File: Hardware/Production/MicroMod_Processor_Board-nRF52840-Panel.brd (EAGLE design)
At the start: 199.6 x 83.1 mm, 454 parts, among them J1 MICROMOD-2222, J10 MICROMOD-2222, J11 MICROMOD-2222, J12 MICROMOD-2222, J13 MICROMOD-2222, J14 MICROMOD-2222, J15 MICROMOD-2222, J16 MICROMOD-2222, J2 MICROMOD-2222, J3 MICROMOD-2222, J4 MICROMOD-2222, J5 MICROMOD-2222, J6 MICROMOD-2222, J7 MICROMOD-2222, J8 MICROMOD-2222, J9 MICROMOD-2222, U1 W25QXX128MBIT-6X5, U10 MDBT50Q, U11 W25QXX128MBIT-6X5, U12 MDBT50Q, U13 W25QXX128MBIT-6X5, U14 MDBT50Q, U15 W25QXX128MBIT-6X5, U16 MDBT50Q, U17 W25QXX128MBIT-6X5, U18 MDBT50Q, U19 W25QXX128MBIT-6X5, U2 MDBT50Q, U20 MDBT50Q, U21 W25QXX128MBIT-6X5, U22 MDBT50Q, U23 W25QXX128MBIT-6X5, U24 MDBT50Q, U25 W25QXX128MBIT-6X5, U26 MDBT50Q, U27 W25QXX128MBIT-6X5, U28 MDBT50Q, U29 W25QXX128MBIT-6X5, U3 W25QXX128MBIT-6X5, U30 MDBT50Q, U31 W25QXX128MBIT-6X5, U32 MDBT50Q, U4 MDBT50Q, U5 W25QXX128MBIT-6X5, U6 MDBT50Q, U7 W25QXX128MBIT-6X5, U8 MDBT50Q, U9 W25QXX128MBIT-6X5, Y1 32.768kHz, Y10 32.768kHz, Y11 32.768kHz, Y12 32.768kHz, Y13 32.768kHz, Y14 32.768kHz, Y15 32.768kHz, Y16 32.768kHz, Y2 32.768kHz, Y3 32.768kHz, Y4 32.768kHz, Y5 32.768kHz, Y6 32.768kHz, Y7 32.768kHz, Y8 32.768kHz, Y9 32.768kHz

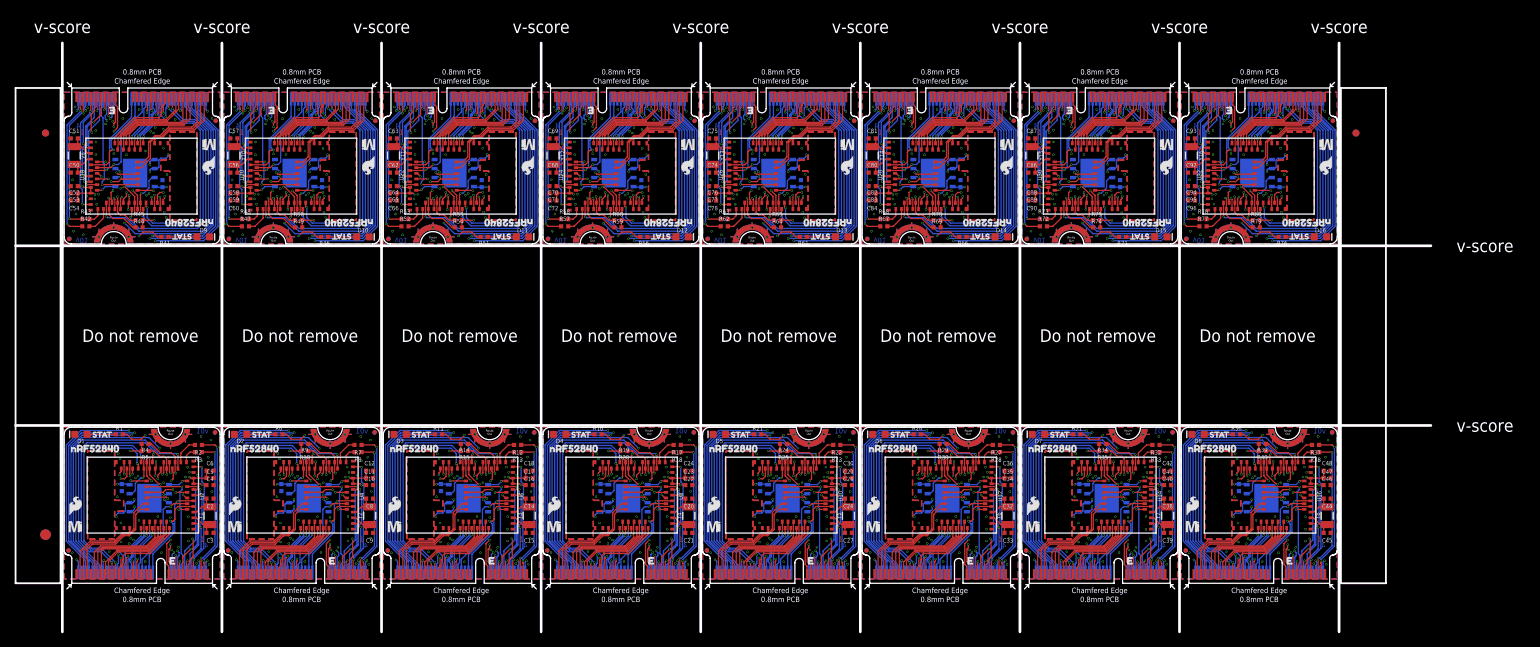
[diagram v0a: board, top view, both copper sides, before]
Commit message: Re-panelized for v10
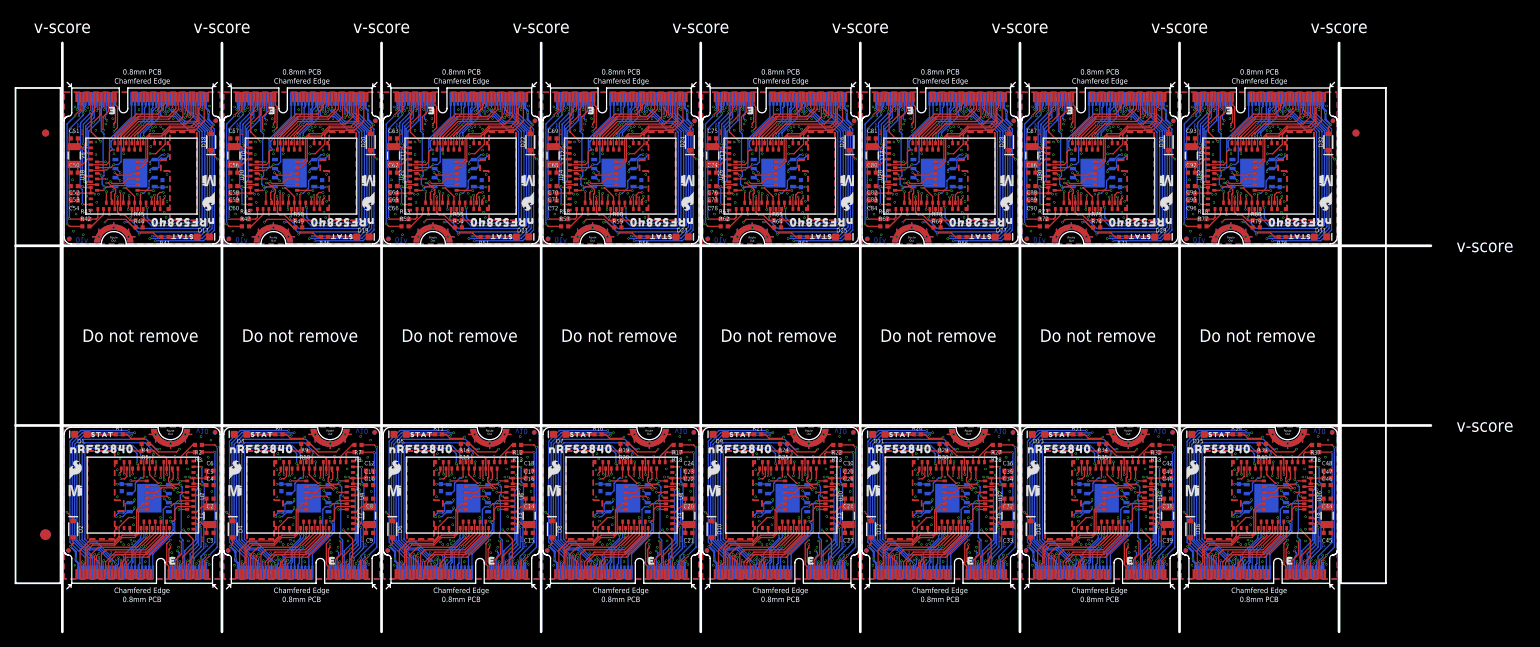
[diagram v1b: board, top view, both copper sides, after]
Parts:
- added D17, D19, D21, D23, D25, D27, D29, D31: BLUE, SparkFun-LED:LED-0603
- added D18, D20, D22, D24, D26, D28, D30, D32: 1A/23V/620mV, SparkFun-DiscreteSemi:SOD-323
- D10, D12, D14, D16, D2, D4, D6, D8: value BLUE -> 1A/23V/620mV; device SparkFun-LED:LED-0603 -> SparkFun-DiscreteSemi:SOD-323
- U$10, U$15, U$20, U$25, U$30, U$35, U$40, U$45, U$50, U$55, U$60, U$65, U$70, U$75, U$80: device buzzard_labels (80):NRF528400 -> output:STAT0
- U$11, U$16, U$21, U$26, U$31, U$36, U$4, U$41, U$46, U$51, U$56, U$61, U$66, U$71, U$76: device SparkFun-Buzzard:STAT_TO_32 -> SparkFun-MicroMod:MICROMOD_MI_LOGO_.35
- U$12, U$17, U$22, U$27, U$32, U$37, U$42, U$47, U$52, U$57, U$62, U$67, U$7, U$72, U$77: device SparkFun-MicroMod:MICROMOD_MI_LOGO_.35 -> SparkFun-MicroMod:MICROMOD_LOGO_.35
- U$13, U$18, U$23, U$28, U$33, U$38, U$43, U$48, U$53, U$58, U$63, U$68, U$73, U$78, U$8: device SparkFun-MicroMod:MICROMOD_LOGO_.35 -> output:NRF528400
- U$14, U$19, U$24, U$29, U$34, U$39, U$44, U$49, U$54, U$59, U$64, U$69, U$74, U$79, U$9: device buzzard_labels (79):NRF528400 -> output:NRF528400
- U$2: device buzzard_labels (79):NRF528400 -> output:STAT0
- U$3: device buzzard_labels (80):NRF528400 -> output:NRF528400
- U$6: device SparkFun-Buzzard:STAT_TO_32 -> output:NRF528400
- moved D8 92.1 mm to (68.8, 7.62), turned to 270 degrees
- moved D9 77.9 mm to (92.4, 21.0), turned to 180 degrees
- moved D6 69.9 mm to (46.3, 7.62), turned to 270 degrees
- moved D7 67.5 mm to (69.9, 21.0)
- moved D10 64.2 mm to (91.3, 7.62), turned to 270 degrees
- moved D11 57.5 mm to (114.9, 21.0), turned to 180 degrees
- moved D12 49.1 mm to (113.8, 7.62), turned to 270 degrees
- moved D4 48.0 mm to (23.8, 7.62), turned to 270 degrees
- moved D16 45.1 mm to (158.8, 7.62), turned to 270 degrees
- moved D5 45.0 mm to (47.4, 21.0)
- moved D14 41.4 mm to (136.3, 7.62), turned to 270 degrees
- moved D13 39.3 mm to (137.4, 21.0), turned to 180 degrees
- moved D15 28.3 mm to (159.9, 21.0), turned to 180 degrees
- moved D2 27.1 mm to (1.27, 7.62), turned to 270 degrees
- moved D3 22.5 mm to (24.9, 21.0)
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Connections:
- net SPI_!CS!16 renamed SPI_!CS1!/SDIO_DATA9
- net SPI_!CS!18 renamed SPI_!CS1!/SDIO_DATA10
- net SPI_!CS!20 renamed SPI_!CS1!/SDIO_DATA11
- net SPI_!CS!22 renamed SPI_!CS1!/SDIO_DATA12
- net SPI_!CS!24 renamed SPI_!CS1!/SDIO_DATA13
- net SPI_!CS!26 renamed SPI_!CS1!/SDIO_DATA14
- net SPI_!CS!28 renamed SPI_!CS1!/SDIO_DATA15
- net SPI_!CS!30 renamed SPI_!CS1!/SDIO_DATA16
- net SPI_MISO1 renamed SPI_CIPO
- net SPI_MISO11 renamed SPI_CIPO5
- net SPI_MISO13 renamed SPI_CIPO6
- net SPI_MISO15 renamed SPI_CIPO7
- net SPI_MISO17 renamed SPI_CIPO8
- net SPI_MISO19 renamed SPI_CIPO9
- net SPI_MISO21 renamed SPI_CIPO10
- net SPI_MISO23 renamed SPI_CIPO11
- net SPI_MISO25 renamed SPI_CIPO12
- net SPI_MISO27 renamed SPI_CIPO13
- net SPI_MISO29 renamed SPI_CIPO14
- net SPI_MISO3 renamed SPI_CIPO1
- net SPI_MISO31 renamed SPI_CIPO15
- net SPI_MISO5 renamed SPI_CIPO2
- net SPI_MISO7 renamed SPI_CIPO3
- net SPI_MISO9 renamed SPI_CIPO4
- net SPI_MOSI1 renamed SPI_COPI
- net SPI_MOSI10 renamed SPI_COPI5
- net SPI_MOSI12 renamed SPI_COPI6
- net SPI_MOSI14 renamed SPI_COPI7
- net SPI_MOSI16 renamed SPI_COPI8
- net SPI_MOSI18 renamed SPI_COPI9
- net SPI_MOSI2 renamed SPI_COPI1
- net SPI_MOSI20 renamed SPI_COPI10
- net SPI_MOSI22 renamed SPI_COPI11
- net SPI_MOSI24 renamed SPI_COPI12
- net SPI_MOSI26 renamed SPI_COPI13
- net SPI_MOSI28 renamed SPI_COPI14
- net SPI_MOSI30 renamed SPI_COPI15
- net SPI_MOSI4 renamed SPI_COPI2
- net SPI_MOSI6 renamed SPI_COPI3
- net SPI_MOSI8 renamed SPI_COPI4
- net SPI_SCK17 renamed SPI_SCK1/SDIO_CLK8
- net SPI_SCK19 renamed SPI_SCK1/SDIO_CLK9
- net SPI_SCK21 renamed SPI_SCK1/SDIO_CLK10
- net SPI_SCK23 renamed SPI_SCK1/SDIO_CLK11
- net SPI_SCK25 renamed SPI_SCK1/SDIO_CLK12
- net SPI_SCK27 renamed SPI_SCK1/SDIO_CLK13
- net SPI_SCK29 renamed SPI_SCK1/SDIO_CLK14
- net SPI_SCK31 renamed SPI_SCK1/SDIO_CLK15
- removed net ADC_D+: J1.63, U2.10
- removed net ADC_D+1: J2.63, U4.10
- removed net ADC_D+10: J11.63, U22.10
- removed net ADC_D+11: J12.63, U24.10
- removed net ADC_D+12: J13.63, U26.10
- removed net ADC_D+13: J14.63, U28.10
- removed net ADC_D+14: J15.63, U30.10
- removed net ADC_D+15: J16.63, U32.10
- removed net ADC_D+2: J3.63, U6.10
- removed net ADC_D+3: J4.63, U8.10
- removed net ADC_D+4: J5.63, U10.10
- removed net ADC_D+5: J6.63, U12.10
- removed net ADC_D+6: J7.63, U14.10
- removed net ADC_D+7: J8.63, U16.10
- removed net ADC_D+8: J9.63, U18.10
- removed net ADC_D+9: J10.63, U20.10
- removed net ADC_D-: J1.65, U2.9
- removed net ADC_D-1: J2.65, U4.9
- removed net ADC_D-10: J11.65, U22.9
- removed net ADC_D-11: J12.65, U24.9
- removed net ADC_D-12: J13.65, U26.9
- removed net ADC_D-13: J14.65, U28.9
- removed net ADC_D-14: J15.65, U30.9
- removed net ADC_D-15: J16.65, U32.9
- removed net ADC_D-2: J3.65, U6.9
- removed net ADC_D-3: J4.65, U8.9
- removed net ADC_D-4: J5.65, U10.9
- removed net ADC_D-5: J6.65, U12.9
- removed net ADC_D-6: J7.65, U14.9
- removed net ADC_D-7: J8.65, U16.9
- removed net ADC_D-8: J9.65, U18.9
- removed net ADC_D-9: J10.65, U20.9
- removed net GPIO0: J1.40, U2.8
- removed net GPIO113: J15.69, U30.56
- removed net GPIO114: J15.71, U30.57
- removed net GPIO115: J15.42, U30.7
- removed net GPIO116: J15.46, U30.5
- removed net GPIO117: J15.44, U30.6
- removed net GPIO118: J15.48, U30.4
- removed net GPIO119: J15.40, U30.8
- removed net GPIO120: J16.73, U32.3
- removed net GPIO121: J16.69, U32.56
- removed net GPIO122: J16.71, U32.57
- removed net GPIO123: J16.42, U32.7
- removed net GPIO124: J16.46, U32.5
- removed net GPIO125: J16.44, U32.6
- removed net GPIO126: J16.48, U32.4
- removed net GPIO127: J16.40, U32.8
- removed net N$11 (its old number): D3.A, R11.1
- removed net N$16 (its old number): D4.A, R16.1
- removed net N$21 (its old number): D5.A, R21.1
- removed net N$26 (its old number): D6.A, R26.1
- removed net N$41 (its old number): D9.A, R41.1
- removed net N$46 (its old number): D10.A, R46.1
- removed net N$51 (its old number): D11.A, R51.1
- removed net N$56 (its old number): D12.A, R56.1
- removed net N$71 (its old number): D15.A, R71.1
- removed net N$76 (its old number): D16.A, R76.1
- removed net NFC1: J1.43, U2.52
- removed net NFC10: J5.41, U10.54
- removed net NFC11: J6.43, U12.52
- removed net NFC12: J6.41, U12.54
- removed net NFC13: J7.43, U14.52
- removed net NFC14: J7.41, U14.54
- removed net NFC15: J8.43, U16.52
- removed net NFC16: J8.41, U16.54
- removed net NFC17: J9.43, U18.52
- removed net NFC18: J9.41, U18.54
- removed net NFC19: J10.43, U20.52
- removed net NFC2: J1.41, U2.54
- removed net NFC20: J10.41, U20.54
- removed net NFC21: J11.43, U22.52
- removed net NFC22: J11.41, U22.54
- removed net NFC23: J12.43, U24.52
- removed net NFC24: J12.41, U24.54
- removed net NFC25: J13.43, U26.52
- removed net NFC26: J13.41, U26.54
- removed net NFC27: J14.43, U28.52
- removed net NFC28: J14.41, U28.54
- removed net NFC29: J15.43, U30.52
- removed net NFC3: J2.43, U4.52
- removed net NFC30: J15.41, U30.54
- removed net NFC31: J16.43, U32.52
- removed net NFC32: J16.41, U32.54
- removed net NFC4: J2.41, U4.54
- removed net NFC5: J3.43, U6.52
- removed net NFC6: J3.41, U6.54
- removed net NFC7: J4.43, U8.52
- removed net NFC8: J4.41, U8.54
- removed net NFC9: J5.43, U10.52
- removed net SPI_!CS!17: J9.55, U18.44
- removed net SPI_!CS!19: J10.55, U20.44
- removed net SPI_!CS!21: J11.55, U22.44
- removed net SPI_!CS!23: J12.55, U24.44
- removed net SPI_!CS!25: J13.55, U26.44
- removed net SPI_!CS!27: J14.55, U28.44
- removed net SPI_!CS!29: J15.55, U30.44
- removed net SPI_!CS!31: J16.55, U32.44
- removed net SPI_MISO: J1.64, U1.5, U2.43
- removed net SPI_MISO10: J6.64, U11.5, U12.43
- removed net SPI_MISO12: J7.64, U13.5, U14.43
- removed net SPI_MISO14: J8.64, U15.5, U16.43
- removed net SPI_MISO16: J9.64, U17.5, U18.43
- removed net SPI_MISO18: J10.64, U19.5, U20.43
- removed net SPI_MISO2: J2.64, U3.5, U4.43
- removed net SPI_MISO20: J11.64, U21.5, U22.43
- removed net SPI_MISO22: J12.64, U23.5, U24.43
- removed net SPI_MISO24: J13.64, U25.5, U26.43
- removed net SPI_MISO26: J14.64, U27.5, U28.43
- removed net SPI_MISO28: J15.64, U29.5, U30.43
- removed net SPI_MISO30: J16.64, U31.5, U32.43
- removed net SPI_MISO4: J3.64, U5.5, U6.43
- removed net SPI_MISO6: J4.64, U7.5, U8.43
- removed net SPI_MISO8: J5.64, U10.43, U9.5
- removed net SPI_MOSI: J1.62, U2.36
- removed net SPI_MOSI11: J6.62, U12.36
- removed net SPI_MOSI13: J7.62, U14.36
- removed net SPI_MOSI15: J8.62, U16.36
- removed net SPI_MOSI17: J9.62, U18.36
- removed net SPI_MOSI19: J10.62, U20.36
- removed net SPI_MOSI21: J11.62, U22.36
- removed net SPI_MOSI23: J12.62, U24.36
- removed net SPI_MOSI25: J13.62, U26.36
- removed net SPI_MOSI27: J14.62, U28.36
- removed net SPI_MOSI29: J15.62, U30.36
- removed net SPI_MOSI3: J2.62, U4.36
- removed net SPI_MOSI31: J16.62, U32.36
- removed net SPI_MOSI5: J3.62, U6.36
- removed net SPI_MOSI7: J4.62, U8.36
- removed net SPI_MOSI9: J5.62, U10.36
- removed net SPI_SCK16: J9.57, U18.13
- removed net SPI_SCK18: J10.57, U20.13
- removed net SPI_SCK20: J11.57, U22.13
- removed net SPI_SCK22: J12.57, U24.13
- removed net SPI_SCK24: J13.57, U26.13
- removed net SPI_SCK26: J14.57, U28.13
- removed net SPI_SCK28: J15.57, U30.13
- removed net SPI_SCK30: J16.57, U32.13
- new net 3.3V_EN: J1.4, U2.8
- new net 3.3V_EN1: J2.4, U4.8
- new net 3.3V_EN10: J11.4, U22.8
- new net 3.3V_EN11: J12.4, U24.8
- new net 3.3V_EN12: J13.4, U26.8
- new net 3.3V_EN13: J14.4, U28.8
- new net 3.3V_EN14: J15.4, U30.8
- new net 3.3V_EN15: J16.4, U32.8
- new net 3.3V_EN2: J3.4, U6.8
- new net 3.3V_EN3: J4.4, U8.8
- new net 3.3V_EN4: J5.4, U10.8
- new net 3.3V_EN5: J6.4, U12.8
- new net 3.3V_EN6: J7.4, U14.8
- new net 3.3V_EN7: J8.4, U16.8
- new net 3.3V_EN8: J9.4, U18.8
- new net 3.3V_EN9: J10.4, U20.8
- new net GPIO0/ADC1: J2.40, U4.10
- new net GPIO0/ADC10: J10.40, U20.10
- new net GPIO0/ADC11: J11.40, U22.10
- new net GPIO0/ADC12: J12.40, U24.10
- new net GPIO0/ADC13: J13.40, U26.10
- new net GPIO0/ADC14: J14.40, U28.10
- new net GPIO0/ADC15: J15.40, U30.10
- new net GPIO0/ADC16: J16.40, U32.10
- new net GPIO0/ADC2: J1.40, U2.10
- new net GPIO0/ADC3: J3.40, U6.10
- new net GPIO0/ADC4: J4.40, U8.10
- new net GPIO0/ADC5: J5.40, U10.10
- new net GPIO0/ADC6: J6.40, U12.10
- new net GPIO0/ADC7: J7.40, U14.10
- new net GPIO0/ADC8: J8.40, U16.10
- new net GPIO0/ADC9: J9.40, U18.10
- new net GPIO1/ADC1: J2.42, U4.9
- new net GPIO1/ADC10: J10.42, U20.9
- new net GPIO1/ADC11: J11.42, U22.9
- new net GPIO1/ADC12: J12.42, U24.9
- new net GPIO1/ADC13: J13.42, U26.9
- new net GPIO1/ADC14: J14.42, U28.9
- new net GPIO1/ADC15: J15.42, U30.9
- new net GPIO1/ADC16: J16.42, U32.9
- new net GPIO1/ADC2: J3.42, U6.9
- new net GPIO1/ADC3: J1.42, U2.9
- new net GPIO1/ADC4: J4.42, U8.9
- new net GPIO1/ADC5: J5.42, U10.9
- new net GPIO1/ADC6: J6.42, U12.9
- new net GPIO1/ADC7: J7.42, U14.9
- new net GPIO1/ADC8: J8.42, U16.9
- new net GPIO1/ADC9: J9.42, U18.9
- new net GPIO10/NFC1: J2.63, U4.54
- new net GPIO10/NFC10: J10.63, U20.54
- new net GPIO10/NFC11: J11.63, U22.54
- new net GPIO10/NFC12: J12.63, U24.54
- new net GPIO10/NFC13: J13.63, U26.54
- new net GPIO10/NFC14: J14.63, U28.54
- new net GPIO10/NFC15: J15.63, U30.54
- new net GPIO10/NFC16: J16.63, U32.54
- new net GPIO10/NFC2: J1.63, U2.54
- new net GPIO10/NFC3: J3.63, U6.54
- new net GPIO10/NFC4: J4.63, U8.54
- new net GPIO10/NFC5: J5.63, U10.54
- new net GPIO10/NFC6: J6.63, U12.54
- new net GPIO10/NFC7: J7.63, U14.54
- new net GPIO10/NFC8: J8.63, U16.54
- new net GPIO10/NFC9: J9.63, U18.54
- new net GPIO9/NFC1: J1.65, U2.52
- new net GPIO9/NFC10: J10.65, U20.52
- new net GPIO9/NFC11: J11.65, U22.52
- new net GPIO9/NFC12: J12.65, U24.52
- new net GPIO9/NFC13: J13.65, U26.52
- new net GPIO9/NFC14: J14.65, U28.52
- new net GPIO9/NFC15: J15.65, U30.52
- new net GPIO9/NFC16: J16.65, U32.52
- new net GPIO9/NFC2: J2.65, U4.52
- new net GPIO9/NFC3: J3.65, U6.52
- new net GPIO9/NFC4: J4.65, U8.52
- new net GPIO9/NFC5: J5.65, U10.52
- new net GPIO9/NFC6: J6.65, U12.52
- new net GPIO9/NFC7: J7.65, U14.52
- new net GPIO9/NFC8: J8.65, U16.52
- new net GPIO9/NFC9: J9.65, U18.52
- new net N$12: D4.A, J2.2, J2.74
- new net N$13: D5.A, R11.1
- new net N$18: D6.A, J3.2, J3.74
- new net N$19: D7.A, R16.1
- new net N$24: D8.A, J4.2, J4.74
- new net N$25: D9.A, R21.1
- new net N$30: D10.A, J5.2, J5.74
- new net N$37: D13.A, R31.1
- new net N$42: D14.A, J7.2, J7.74
- new net N$43: D15.A, R36.1
- new net N$48: D16.A, J8.2, J8.74
- new net N$49: D17.A, R41.1
- new net N$54: D18.A, J9.2, J9.74
- new net N$55: D19.A, R46.1
- new net N$60: D20.A, J10.2, J10.74
- new net N$67: D23.A, R56.1
- new net N$7: D3.A, R6.1
- new net N$72: D24.A, J12.2, J12.74
- new net N$73: D25.A, R61.1
- new net N$78: D26.A, J13.2, J13.74
- new net N$79: D27.A, R66.1
- new net N$84: D28.A, J14.2, J14.74
- new net N$85: D29.A, R71.1
- new net N$90: D30.A, J15.2, J15.74
- new net N$91: D31.A, R76.1
- new net N$96: D32.A, J16.2, J16.74
- new net SPI_!CS1!/SDIO_DATA1: J2.70, U3.7, U4.47
- new net SPI_!CS1!/SDIO_DATA2: J3.70, U5.7, U6.47
- new net SPI_!CS1!/SDIO_DATA3: J1.70, U1.7, U2.47
- new net SPI_!CS1!/SDIO_DATA4: J4.70, U7.7, U8.47
- new net SPI_!CS1!/SDIO_DATA5: J5.70, U10.47, U9.7
- new net SPI_!CS1!/SDIO_DATA6: J6.70, U11.7, U12.47
- new net SPI_!CS1!/SDIO_DATA7: J7.70, U13.7, U14.47
- new net SPI_!CS1!/SDIO_DATA8: J8.70, U15.7, U16.47
- new net SPI_CIPO1/SDIO_DATA0: J1.64, U1.2, U2.43
- new net SPI_CIPO1/SDIO_DATA1: J2.64, U3.2, U4.43
- new net SPI_CIPO1/SDIO_DATA10: J11.64, U21.2, U22.43
- new net SPI_CIPO1/SDIO_DATA11: J12.64, U23.2, U24.43
- new net SPI_CIPO1/SDIO_DATA12: J13.64, U25.2, U26.43
- new net SPI_CIPO1/SDIO_DATA13: J14.64, U27.2, U28.43
- new net SPI_CIPO1/SDIO_DATA14: J15.64, U29.2, U30.43
- new net SPI_CIPO1/SDIO_DATA15: J16.64, U31.2, U32.43
- new net SPI_CIPO1/SDIO_DATA2: J3.64, U5.2, U6.43
- new net SPI_CIPO1/SDIO_DATA3: J4.64, U7.2, U8.43
- new net SPI_CIPO1/SDIO_DATA4: J5.64, U10.43, U9.2
- new net SPI_CIPO1/SDIO_DATA5: J6.64, U11.2, U12.43
- new net SPI_CIPO1/SDIO_DATA6: J7.64, U13.2, U14.43
- new net SPI_CIPO1/SDIO_DATA7: J8.64, U15.2, U16.43
- new net SPI_CIPO1/SDIO_DATA8: J9.64, U17.2, U18.43
- new net SPI_CIPO1/SDIO_DATA9: J10.64, U19.2, U20.43
- new net SPI_COPI1/SDIO_CMD: J1.62, U1.5, U2.36
- new net SPI_COPI1/SDIO_CMD1: J2.62, U3.5, U4.36
- new net SPI_COPI1/SDIO_CMD10: J11.62, U21.5, U22.36
- new net SPI_COPI1/SDIO_CMD11: J12.62, U23.5, U24.36
- new net SPI_COPI1/SDIO_CMD12: J13.62, U25.5, U26.36
- new net SPI_COPI1/SDIO_CMD13: J14.62, U27.5, U28.36
- new net SPI_COPI1/SDIO_CMD14: J15.62, U29.5, U30.36
- new net SPI_COPI1/SDIO_CMD15: J16.62, U31.5, U32.36
- new net SPI_COPI1/SDIO_CMD2: J3.62, U5.5, U6.36
- new net SPI_COPI1/SDIO_CMD3: J4.62, U7.5, U8.36
- new net SPI_COPI1/SDIO_CMD4: J5.62, U10.36, U9.5
- new net SPI_COPI1/SDIO_CMD5: J6.62, U11.5, U12.36
- new net SPI_COPI1/SDIO_CMD6: J7.62, U13.5, U14.36
- new net SPI_COPI1/SDIO_CMD7: J8.62, U15.5, U16.36
- new net SPI_COPI1/SDIO_CMD8: J9.62, U17.5, U18.36
- new net SPI_COPI1/SDIO_CMD9: J10.62, U19.5, U20.36
- new net SPI_SCK1/SDIO_CLK: J1.60, U1.6, U2.42
- new net SPI_SCK1/SDIO_CLK1: J2.60, U3.6, U4.42
- new net SPI_SCK1/SDIO_CLK2: J3.60, U5.6, U6.42
- new net SPI_SCK1/SDIO_CLK3: J4.60, U7.6, U8.42
- new net SPI_SCK1/SDIO_CLK4: J5.60, U10.42, U9.6
- new net SPI_SCK1/SDIO_CLK5: J6.60, U11.6, U12.42
- new net SPI_SCK1/SDIO_CLK6: J7.60, U13.6, U14.42
- new net SPI_SCK1/SDIO_CLK7: J8.60, U15.6, U16.42
- net !BOOT!: now also U2.23; no longer U2.37
- net !BOOT!1: now also U4.23; no longer U4.37
- net !BOOT!10: now also U22.23; no longer U22.37
- net !BOOT!11: now also U24.23; no longer U24.37
- net !BOOT!12: now also U26.23; no longer U26.37
- net !BOOT!13: now also U28.23; no longer U28.37
- net !BOOT!14: now also U30.23; no longer U30.37
- net !BOOT!15: now also U32.23; no longer U32.37
- net !BOOT!2: now also U6.23; no longer U6.37
- net !BOOT!3: now also U8.23; no longer U8.37
- net !BOOT!4: now also U10.23; no longer U10.37
- net !BOOT!5: now also U12.23; no longer U12.37
- net !BOOT!6: now also U14.23; no longer U14.37
- net !BOOT!7: now also U16.23; no longer U16.37
- net !BOOT!8: now also U18.23; no longer U18.37
- net !BOOT!9: now also U20.23; no longer U20.37
- net 3.3V: now also D2.C, J1.72; no longer J1.2, J1.74
- net 3.3V1: now also D4.C, J2.72; no longer J2.2, J2.74
- net 3.3V10: now also D22.C, J11.72; no longer J11.2, J11.74
- net 3.3V11: now also D24.C, J12.72; no longer J12.2, J12.74
- net 3.3V12: now also D26.C, J13.72; no longer J13.2, J13.74
- net 3.3V13: now also D28.C, J14.72; no longer J14.2, J14.74
- net 3.3V14: now also D30.C, J15.72; no longer J15.2, J15.74
- net 3.3V15: now also D32.C, J16.72; no longer J16.2, J16.74
- net 3.3V2: now also D6.C, J3.72; no longer J3.2, J3.74
- net 3.3V3: now also D8.C, J4.72; no longer J4.2, J4.74
- net 3.3V4: now also D10.C, J5.72; no longer J5.2, J5.74
- net 3.3V5: now also D12.C, J6.72; no longer J6.2, J6.74
- net 3.3V6: now also D14.C, J7.72; no longer J7.2, J7.74
- net 3.3V7: now also D16.C, J8.72; no longer J8.2, J8.74
- net 3.3V8: now also D18.C, J9.72; no longer J9.2, J9.74
- net 3.3V9: now also D20.C, J10.72; no longer J10.2, J10.74
- net GND1: now also D3.C; no longer D2.C
- net GND10: now also D21.C; no longer D11.C
- net GND11: now also D23.C; no longer D12.C
- net GND12: now also D25.C; no longer D13.C
- net GND13: now also D27.C; no longer D14.C
- net GND14: now also D29.C; no longer D15.C
- net GND15: now also D31.C; no longer D16.C
- net GND2: now also D5.C; no longer D3.C
- net GND3: now also D7.C; no longer D4.C
- net GND4: now also D9.C; no longer D5.C
- net GND5: now also D11.C; no longer D6.C
- net GND6: now also D13.C; no longer D7.C
- net GND7: now also D15.C; no longer D8.C
- net GND8: now also D17.C; no longer D9.C
- net GND9: now also D19.C; no longer D10.C
- net GPIO1: now also J2.73, U4.41; no longer J1.42, U2.7
- net GPIO100: now also J15.69, U30.56; no longer J13.46, U26.5
- net GPIO101: now also J15.71, U30.57; no longer J13.44, U26.6
- net GPIO102: now also J15.46, U30.5; no longer J13.48, U26.4
- net GPIO103: now also J15.44, U30.6; no longer J13.40, U26.8
- net GPIO104: now also J15.48, U30.4; no longer J14.73, U28.3
- net GPIO105: now also J15.67, U30.7; no longer J14.69, U28.56
- net GPIO106: now also J16.73, U32.41; no longer J14.71, U28.57
- net GPIO107: now also J16.69, U32.56; no longer J14.42, U28.7
- net GPIO108: now also J16.71, U32.57; no longer J14.46, U28.5
- net GPIO109: now also J16.46, U32.5; no longer J14.44, U28.6
- net GPIO11: now also J2.46, U4.5; no longer J2.42, U4.7
- net GPIO110: now also J16.44, U32.6; no longer J14.48, U28.4
- net GPIO111: now also J16.48, U32.4; no longer J14.40, U28.8
- net GPIO112: now also J16.67, U32.7; no longer J15.73, U30.3
- net GPIO12: now also J2.44, U4.6; no longer J2.46, U4.5
- net GPIO13: now also J2.48, U4.4; no longer J2.44, U4.6
- net GPIO14: now also J2.67, U4.7; no longer J2.48, U4.4
- net GPIO15: now also J3.73, U6.41; no longer J2.40, U4.8
- net GPIO16: now also J3.69, U6.56; no longer J3.73, U6.3
- net GPIO17: now also J3.71, U6.57; no longer J3.69, U6.56
- net GPIO18: now also J3.46, U6.5; no longer J3.71, U6.57
- net GPIO19: now also J3.44, U6.6; no longer J3.42, U6.7
- net GPIO20: now also J3.48, U6.4; no longer J3.46, U6.5
- net GPIO21: now also J3.67, U6.7; no longer J3.44, U6.6
- net GPIO22: now also J4.73, U8.41; no longer J3.48, U6.4
- net GPIO23: now also J4.69, U8.56; no longer J3.40, U6.8
- net GPIO24: now also J4.71, U8.57; no longer J4.73, U8.3
- net GPIO25: now also J4.46, U8.5; no longer J4.69, U8.56
- net GPIO26: now also J4.44, U8.6; no longer J4.71, U8.57
- net GPIO27: now also J4.48, U8.4; no longer J4.42, U8.7
- net GPIO28: now also J4.67, U8.7; no longer J4.46, U8.5
- net GPIO29: now also J5.73, U10.41; no longer J4.44, U8.6
- net GPIO30: now also J5.69, U10.56; no longer J4.48, U8.4
- net GPIO31: now also J5.71, U10.57; no longer J4.40, U8.8
- net GPIO32: now also J5.46, U10.5; no longer J5.73, U10.3
- net GPIO33: now also J5.44, U10.6; no longer J5.69, U10.56
- net GPIO34: now also J5.48, U10.4; no longer J5.71, U10.57
- net GPIO35: now also J5.67; no longer J5.42
- net GPIO36: now also J6.73, U12.41; no longer J5.46, U10.5
- net GPIO37: now also J6.69, U12.56; no longer J5.44, U10.6
- net GPIO38: now also J6.71, U12.57; no longer J5.48, U10.4
- net GPIO39: now also J6.46, U12.5; no longer J5.40, U10.8
- net GPIO40: now also J6.44, U12.6; no longer J6.73, U12.3
- net GPIO41: now also J6.48, U12.4; no longer J6.69, U12.56
- net GPIO42: now also J6.67, U12.7; no longer J6.71, U12.57
- net GPIO43: now also J7.73, U14.41; no longer J6.42, U12.7
- net GPIO44: now also J7.69, U14.56; no longer J6.46, U12.5
- net GPIO45: now also J7.71, U14.57; no longer J6.44, U12.6
- net GPIO46: now also J7.46, U14.5; no longer J6.48, U12.4
- net GPIO47: now also J7.44, U14.6; no longer J6.40, U12.8
- net GPIO48: now also J7.48, U14.4; no longer J7.73, U14.3
- net GPIO49: now also J7.67, U14.7; no longer J7.69, U14.56
- net GPIO5: now also U2.41; no longer U2.3
- net GPIO50: now also J8.73, U16.41; no longer J7.71, U14.57
- net GPIO51: now also J8.69, U16.56; no longer J7.42, U14.7
- net GPIO52: now also J8.71, U16.57; no longer J7.46, U14.5
- net GPIO53: now also J8.46, U16.5; no longer J7.44, U14.6
- net GPIO54: now also J8.44, U16.6; no longer J7.48, U14.4
- net GPIO55: now also J8.48, U16.4; no longer J7.40, U14.8
- net GPIO56: now also J8.67, U16.7; no longer J8.73, U16.3
- net GPIO57: now also J9.73, U18.41; no longer J8.69, U16.56
- net GPIO58: now also J9.69, U18.56; no longer J8.71, U16.57
- net GPIO59: now also J9.71, U18.57; no longer J8.42, U16.7
- net GPIO60: now also J9.46, U18.5; no longer J8.46, U16.5
- net GPIO61: now also J9.44, U18.6; no longer J8.44, U16.6
- net GPIO62: now also J9.48, U18.4; no longer J8.48, U16.4
- net GPIO63: now also J9.67, U18.7; no longer J8.40, U16.8
- net GPIO64: now also J10.73, U20.41; no longer J9.73, U18.3
- net GPIO65: now also J10.69, U20.56; no longer J9.69, U18.56
- net GPIO66: now also J10.71, U20.57; no longer J9.71, U18.57
- net GPIO67: now also J10.46, U20.5; no longer J9.42, U18.7
- net GPIO68: now also J10.44, U20.6; no longer J9.46, U18.5
- net GPIO69: now also J10.48, U20.4; no longer J9.44, U18.6
- net GPIO70: now also J10.67, U20.7; no longer J9.48, U18.4
- net GPIO71: now also J11.73, U22.41; no longer J9.40, U18.8
- net GPIO72: now also J11.69, U22.56; no longer J10.73, U20.3
- net GPIO73: now also J11.71, U22.57; no longer J10.69, U20.56
- net GPIO74: now also J11.46, U22.5; no longer J10.71, U20.57
- net GPIO75: now also J11.44, U22.6; no longer J10.42, U20.7
- net GPIO76: now also J11.48, U22.4; no longer J10.46, U20.5
- net GPIO77: now also J11.67, U22.7; no longer J10.44, U20.6
- net GPIO78: now also J12.73, U24.41; no longer J10.48, U20.4
- net GPIO79: now also J12.69, U24.56; no longer J10.40, U20.8
- net GPIO8: now also J1.67, U2.7; no longer J2.73, U4.3
- net GPIO80: now also J12.71, U24.57; no longer J11.73, U22.3
- net GPIO81: now also J12.46, U24.5; no longer J11.69, U22.56
- net GPIO82: now also J12.44, U24.6; no longer J11.71, U22.57
- net GPIO83: now also J12.48, U24.4; no longer J11.42, U22.7
- net GPIO84: now also J12.67, U24.7; no longer J11.46, U22.5
- net GPIO85: now also J13.73, U26.41; no longer J11.44, U22.6
- net GPIO86: now also J13.69, U26.56; no longer J11.48, U22.4
- net GPIO87: now also J13.71, U26.57; no longer J11.40, U22.8
- net GPIO88: now also J13.46, U26.5; no longer J12.73, U24.3
- net GPIO89: now also J13.44, U26.6; no longer J12.69, U24.56
- net GPIO90: now also J13.48, U26.4; no longer J12.71, U24.57
- net GPIO91: now also J13.67, U26.7; no longer J12.42, U24.7
- net GPIO92: now also J14.73, U28.41; no longer J12.46, U24.5
- net GPIO93: now also J14.69, U28.56; no longer J12.44, U24.6
- net GPIO94: now also J14.71, U28.57; no longer J12.48, U24.4
- net GPIO95: now also J14.46, U28.5; no longer J12.40, U24.8
- net GPIO96: now also J14.44, U28.6; no longer J13.73, U26.3
- net GPIO97: now also J14.48, U28.4; no longer J13.69, U26.56
- net GPIO98: now also J14.67, U28.7; no longer J13.71, U26.57
- net GPIO99: now also J15.73, U30.41; no longer J13.42, U26.7
- net I2C_!INT!: now also U2.39; no longer U2.60
- net I2C_!INT!1: now also U4.39; no longer U4.60
- net I2C_!INT!10: now also U22.39; no longer U22.60
- net I2C_!INT!11: now also U24.39; no longer U24.60
- net I2C_!INT!12: now also U26.39; no longer U26.60
- net I2C_!INT!13: now also U28.39; no longer U28.60
- net I2C_!INT!14: now also U30.39; no longer U30.60
- net I2C_!INT!15: now also U32.39; no longer U32.60
- net I2C_!INT!2: now also U6.39; no longer U6.60
- net I2C_!INT!3: now also U8.39; no longer U8.60
- net I2C_!INT!4: now also U10.39; no longer U10.60
- net I2C_!INT!5: now also U12.39; no longer U12.60
- net I2C_!INT!6: now also U14.39; no longer U14.60
- net I2C_!INT!7: now also U16.39; no longer U16.60
- net I2C_!INT!8: now also U18.39; no longer U18.60
- net I2C_!INT!9: now also U20.39; no longer U20.60
- net LED_BUILTIN: now also U2.37; no longer U2.23
- net LED_BUILTIN1: now also U4.37; no longer U4.23
- net LED_BUILTIN10: now also U22.37; no longer U22.23
- net LED_BUILTIN11: now also U24.37; no longer U24.23
- net LED_BUILTIN12: now also U26.37; no longer U26.23
- net LED_BUILTIN13: now also U28.37; no longer U28.23
- net LED_BUILTIN14: now also U30.37; no longer U30.23
- net LED_BUILTIN15: now also U32.37; no longer U32.23
- net LED_BUILTIN2: now also U6.37; no longer U6.23
- net LED_BUILTIN3: now also U8.37; no longer U8.23
- net LED_BUILTIN4: now also U10.37; no longer U10.23
- net LED_BUILTIN5: now also U12.37; no longer U12.23
- net LED_BUILTIN6: now also U14.37; no longer U14.23
- net LED_BUILTIN7: now also U16.37; no longer U16.23
- net LED_BUILTIN8: now also U18.37; no longer U18.23
- net LED_BUILTIN9: now also U20.37; no longer U20.23
- net N$31: now also D11.A, R26.1; no longer D7.A, R31.1
- net N$36: now also D12.A, J6.2, J6.74; no longer D8.A, R36.1
- net N$5: now also J1.2, J1.74; no longer R6.1
- net N$61: now also D21.A, R51.1; no longer D13.A, R61.1
- net N$66: now also D22.A, J11.2, J11.74; no longer D14.A, R66.1
- net RX1: now also U2.3; no longer U2.41
- net RX11: now also U12.3; no longer U12.41
- net RX13: now also U14.3; no longer U14.41
- net RX15: now also U16.3; no longer U16.41
- net RX17: now also U18.3; no longer U18.41
- net RX19: now also U20.3; no longer U20.41
- net RX21: now also U22.3; no longer U22.41
- net RX23: now also U24.3; no longer U24.41
- net RX25: now also U26.3; no longer U26.41
- net RX27: now also U28.3; no longer U28.41
- net RX29: now also U30.3; no longer U30.41
- net RX3: now also U4.3; no longer U4.41
- net RX31: now also U32.3; no longer U32.41
- net RX5: now also U6.3; no longer U6.41
- net RX7: now also U8.3; no longer U8.41
- net RX9: now also U10.3; no longer U10.41
- net SDIO_DATA1: no longer U1.2
- net SDIO_DATA11: no longer U11.2
- net SDIO_DATA13: no longer U13.2
- net SDIO_DATA15: no longer U15.2
- net SDIO_DATA17: no longer U17.2
- net SDIO_DATA19: no longer U19.2
- net SDIO_DATA21: no longer U21.2
- net SDIO_DATA23: no longer U23.2
- net SDIO_DATA25: no longer U25.2
- net SDIO_DATA27: no longer U27.2
- net SDIO_DATA29: no longer U29.2
- net SDIO_DATA3: no longer U3.2
- net SDIO_DATA31: no longer U31.2
- net SDIO_DATA5: no longer U5.2
- net SDIO_DATA7: no longer U7.2
- net SDIO_DATA9: no longer U9.2
- net SPI_!CS!: now also J1.55, U2.44; no longer J1.70, U1.7, U2.47
- net SPI_!CS!1: now also J2.55, U4.44; no longer J1.55, U2.44
- net SPI_!CS!10: now also J11.55, U22.44; no longer J6.70, U11.7, U12.47
- net SPI_!CS!11: now also J12.55, U24.44; no longer J6.55, U12.44
- net SPI_!CS!12: now also J13.55, U26.44; no longer J7.70, U13.7, U14.47
- net SPI_!CS!13: now also J14.55, U28.44; no longer J7.55, U14.44
- net SPI_!CS!14: now also J15.55, U30.44; no longer J8.70, U15.7, U16.47
- net SPI_!CS!15: now also J16.55, U32.44; no longer J8.55, U16.44
- net SPI_!CS!2: now also J3.55, U6.44; no longer J2.70, U3.7, U4.47
- net SPI_!CS!3: now also J4.55, U8.44; no longer J2.55, U4.44
- net SPI_!CS!4: now also J5.55, U10.44; no longer J3.70, U5.7, U6.47
- net SPI_!CS!5: now also J6.55, U12.44; no longer J3.55, U6.44
- net SPI_!CS!6: now also J7.55, U14.44; no longer J4.70, U7.7, U8.47
- net SPI_!CS!7: now also J8.55, U16.44; no longer J4.55, U8.44
- net SPI_!CS!8: now also J9.55, U18.44; no longer J5.70, U10.47, U9.7
- net SPI_!CS!9: now also J10.55, U20.44; no longer J5.55, U10.44
- net SPI_SCK: now also J1.57, U2.13; no longer J1.60, U1.6, U2.42
- net SPI_SCK1: now also J2.57, U4.13; no longer J1.57, U2.13
- net SPI_SCK10: now also J11.57, U22.13; no longer J6.57, U12.13
- net SPI_SCK11: now also J12.57, U24.13; no longer J6.60, U11.6, U12.42
- net SPI_SCK12: now also J13.57, U26.13; no longer J7.57, U14.13
- net SPI_SCK13: now also J14.57, U28.13; no longer J7.60, U13.6, U14.42
- net SPI_SCK14: now also J15.57, U30.13; no longer J8.57, U16.13
- net SPI_SCK15: now also J16.57, U32.13; no longer J8.60, U15.6, U16.42
- net SPI_SCK2: now also J3.57, U6.13; no longer J2.57, U4.13
- net SPI_SCK3: now also J4.57, U8.13; no longer J2.60, U3.6, U4.42
- net SPI_SCK4: now also J5.57, U10.13; no longer J3.57, U6.13
- net SPI_SCK5: now also J6.57, U12.13; no longer J3.60, U5.6, U6.42
- net SPI_SCK6: now also J7.57, U14.13; no longer J4.57, U8.13
- net SPI_SCK7: now also J8.57, U16.13; no longer J4.60, U7.6, U8.42
- net SPI_SCK8: now also J9.57, U18.13; no longer J5.57, U10.13
- net SPI_SCK9: now also J10.57, U20.13; no longer J5.60, U10.42, U9.6
- net TX1: now also U2.60; no longer U2.39
- net TX11: now also U12.60; no longer U12.39
- net TX13: now also U14.60; no longer U14.39
- net TX15: now also U16.60; no longer U16.39
- net TX17: now also U18.60; no longer U18.39
- net TX19: now also U20.60; no longer U20.39
- net TX21: now also U22.60; no longer U22.39
- net TX23: now also U24.60; no longer U24.39
- net TX25: now also U26.60; no longer U26.39
- net TX27: now also U28.60; no longer U28.39
- net TX29: now also U30.60; no longer U30.39
- net TX3: now also U4.60; no longer U4.39
- net TX31: now also U32.60; no longer U32.39
- net TX5: now also U6.60; no longer U6.39
- net TX7: now also U8.60; no longer U8.39
- net TX9: now also U10.60; no longer U10.39
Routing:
- net SPI_MISO30: track 44.8 -> 0.00 mm, vias 5 -> 0
- net SPI_MISO28: track 44.8 -> 0.00 mm, vias 5 -> 0
- net SPI_MISO6: track 44.8 -> 0.00 mm, vias 5 -> 0
- net SPI_MISO4: track 44.8 -> 0.00 mm, vias 5 -> 0
- net SPI_MISO2: track 44.8 -> 0.00 mm, vias 5 -> 0
- net SPI_MISO14: track 44.8 -> 0.00 mm, vias 5 -> 0
- net SPI_MISO12: track 44.8 -> 0.00 mm, vias 5 -> 0
- net SPI_MISO18: track 44.8 -> 0.00 mm, vias 5 -> 0
- net SPI_MISO8: track 44.8 -> 0.00 mm, vias 5 -> 0
- net SPI_MISO26: track 44.8 -> 0.00 mm, vias 5 -> 0
- net SPI_MISO20: track 44.8 -> 0.00 mm, vias 5 -> 0
- net SPI_MISO: track 44.8 -> 0.00 mm, vias 5 -> 0
- net SPI_MISO16: track 44.8 -> 0.00 mm, vias 5 -> 0
- net SPI_MISO24: track 44.8 -> 0.00 mm, vias 5 -> 0
- net SPI_MISO22: track 44.8 -> 0.00 mm, vias 5 -> 0
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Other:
- board text added: "v10"
- board text removed: "v01"
